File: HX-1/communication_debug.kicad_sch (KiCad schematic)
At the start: 0 parts

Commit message: move components to correct sheets, change net labels to global
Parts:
- added D1, D2: D_Schottky, symbol Device:D_Schottky
- added JP1: 5V_USB_Solder_Bridge, Jumper:SolderJumper-2_P1.3mm_Bridged_RoundedPad1.0x1.5mm, symbol Jumper:SolderJumper_2_Bridged
- added P1: USB_C_Plug_USB2.0, symbol Connector:USB_C_Plug_USB2.0
- added R2: 10k, Resistor_SMD:R_0603_1608Metric, symbol Device:R
- added R3: 20k, Resistor_SMD:R_0603_1608Metric, symbol Device:R
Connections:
- new net: D1.1 (K), JP1.1 (A)
- new net +5V: JP1.2 (B)
- new net GND: P1.A1 (GND), P1.A12 (GND), P1.B1 (GND), P1.B12 (GND), R3.2
- new net USB_FS_D+: P1.A6 (D+)
- new net USB_FS_D-: P1.A7 (D-)
- new net USB_VBUS_Sensing: D2.1 (K)
- new net VBUS: D1.2 (A), P1.A4 (VBUS), P1.A9 (VBUS), P1.B4 (VBUS), P1.B9 (VBUS), R2.1
- new net vbus_r_divider: D2.2 (A), R2.2, R3.1
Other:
- note added: "TODO: add VBUS LED"

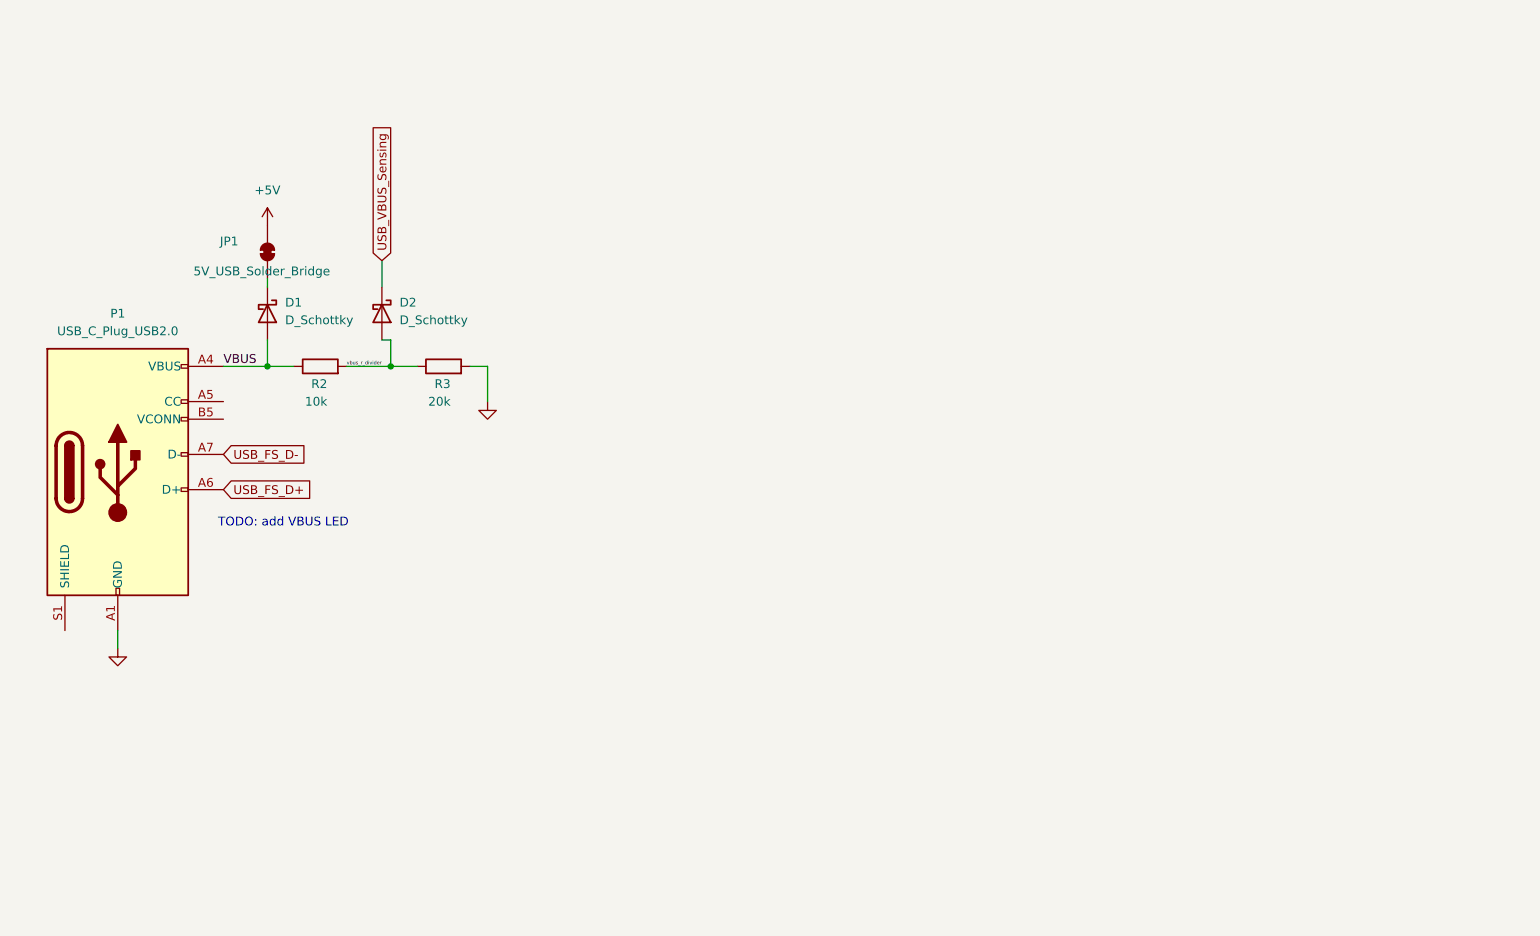
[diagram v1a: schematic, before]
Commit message: add first draft of USB C design
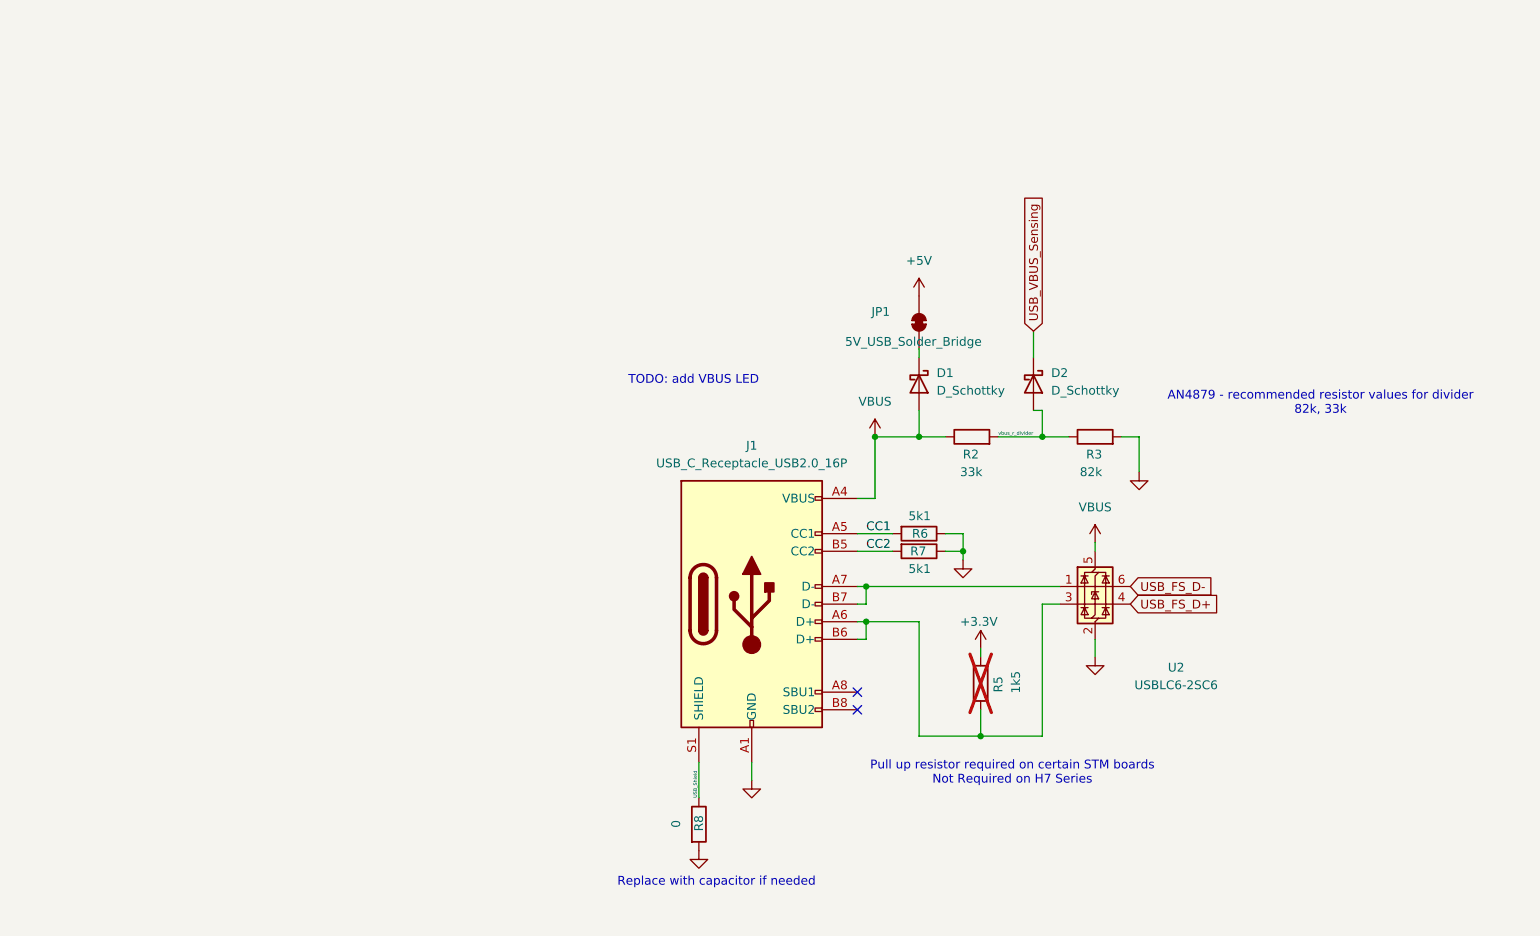
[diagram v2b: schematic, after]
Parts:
- removed P1: USB_C_Plug_USB2.0, symbol Connector:USB_C_Plug_USB2.0
- added J1: USB_C_Receptacle_USB2.0_16P, Connector_USB:USB_C_Receptacle_G-Switch_GT-USB-7010ASV, symbol Connector:USB_C_Receptacle_USB2.0_16P
- added R5: 1k5, Resistor_SMD:R_0603_1608Metric, symbol Device:R
- added R6, R7: 5k1, Resistor_SMD:R_0603_1608Metric, symbol Device:R
- added R8: 0, Resistor_SMD:R_0603_1608Metric, symbol Device:R
- added U2: USBLC6-2SC6, Package_TO_SOT_SMD:SOT-23-6, symbol Power_Protection:USBLC6-2SC6
- D1, D2: footprint (none) -> Diode_SMD:D_SOD-323F; LCSC PN (none) -> C146335
- R2: value 10k -> 33k; LCSC PN C3017715 -> (none)
- R3: value 20k -> 82k
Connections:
- net GND: now also J1.A1 (GND), J1.A12 (GND), J1.B1 (GND), J1.B12 (GND), R6.1, R7.1, R8.2, U2.2 (GND)
- net USB_FS_D+: now also U2.4 (I/O2)
- net USB_FS_D-: now also U2.6 (I/O1)
- net VBUS: now also J1.A4 (VBUS), J1.A9 (VBUS), J1.B4 (VBUS), J1.B9 (VBUS), U2.5 (VBUS)
- new net: J1.A6 (D+), J1.B6 (D+), R5.1, U2.3 (I/O2)
- new net: J1.A7 (D-), J1.B7 (D-), U2.1 (I/O1)
- new net +3.3V: R5.2
- new net CC1: J1.A5 (CC1), R6.2
- new net CC2: J1.B5 (CC2), R7.2
- new net USB_Shield: J1.S1 (SHIELD), R8.1
- no-connect marks 0 -> 2
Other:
- note added: "AN4879 - recommended resistor values for divider 82k, 33k"
- note added: "Pull up resistor required on certain STM boards Not Required on H7 Series"
- note added: "Replace with capacitor if needed"
- moved on the sheet: JP1, R2, R3

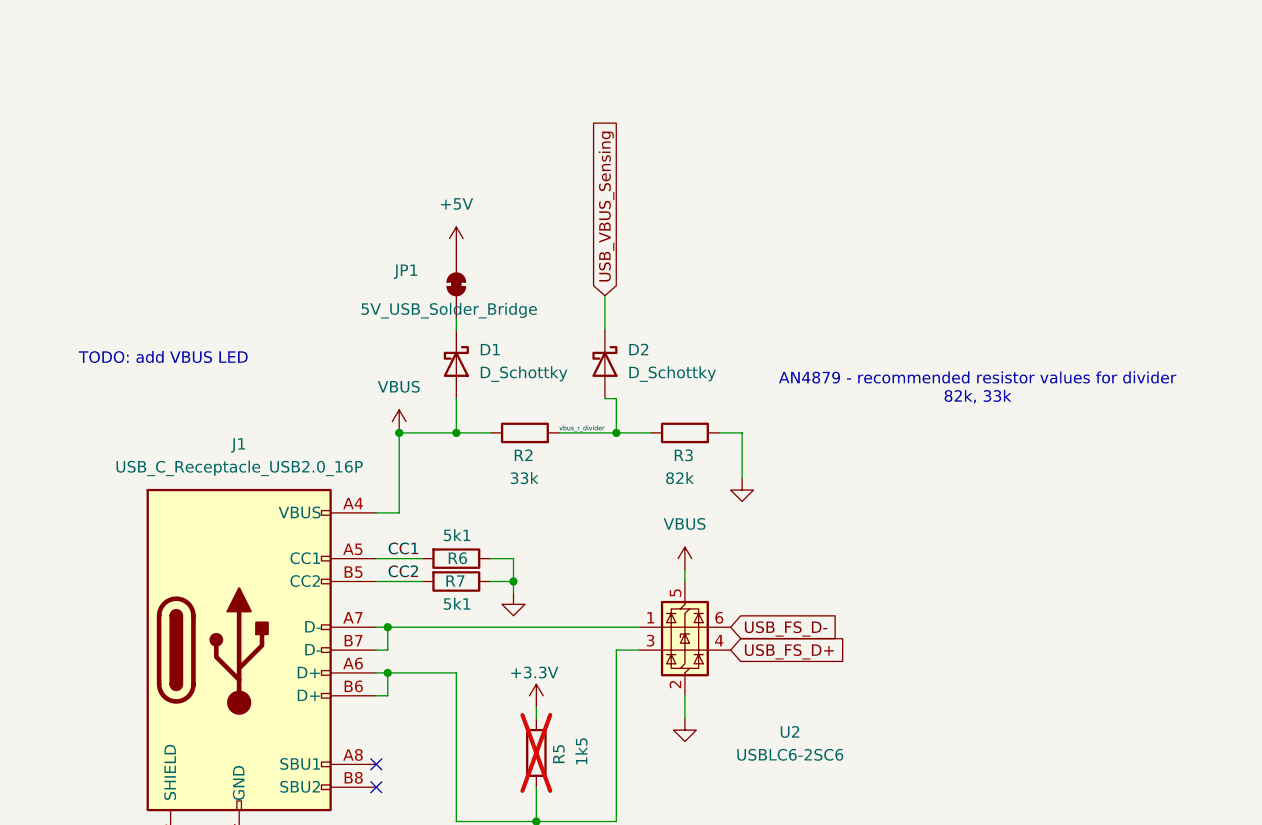
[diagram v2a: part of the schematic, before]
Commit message: add LED and remaining footprints/LCSC PN to USB C circuit
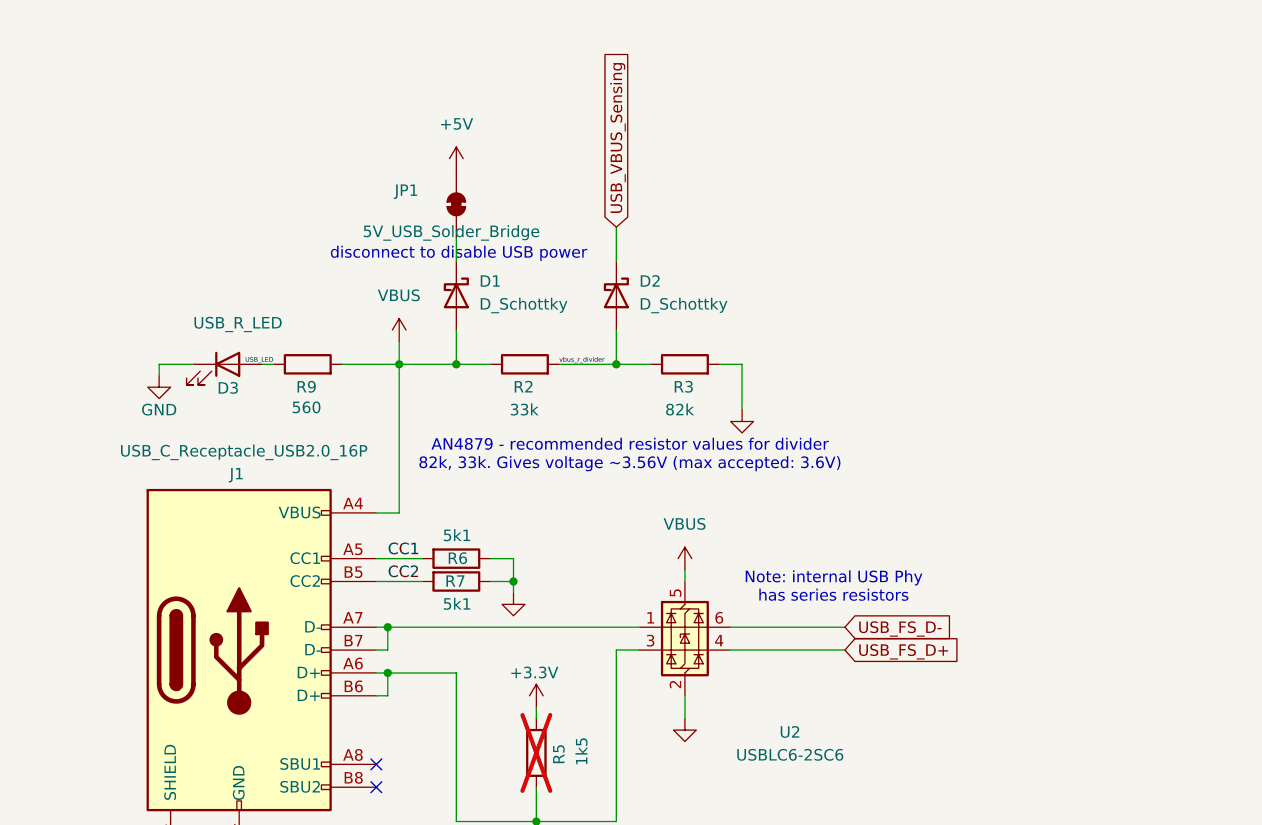
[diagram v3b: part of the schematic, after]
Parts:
- added D3: USB_R_LED, LED_SMD:LED_0603_1608Metric, symbol Device:LED
- added R9: 560, Resistor_SMD:R_0603_1608Metric, symbol Device:R
- R2: LCSC PN (none) -> C4216
- R3: LCSC PN (none) -> C23254
- R6, R7: LCSC PN (none) -> C23186
- R8: LCSC PN (none) -> C21189
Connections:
- net GND: now also D3.1 (K)
- net VBUS: now also R9.2
- new net USB_LED: D3.2 (A), R9.1
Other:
- note added: "AN4879 - recommended resistor values for divider 82k, 33k. Gives voltage ~3.56V (max accepted: 3.6V)"
- note added: "Note: internal USB Phy has series resistors"
- note added: "disconnect to disable USB power"
- note removed: "AN4879 - recommended resistor values for divider 82k, 33k"
- note removed: "TODO: add VBUS LED"
- moved on the sheet: D1, D2, JP1, R2, R3

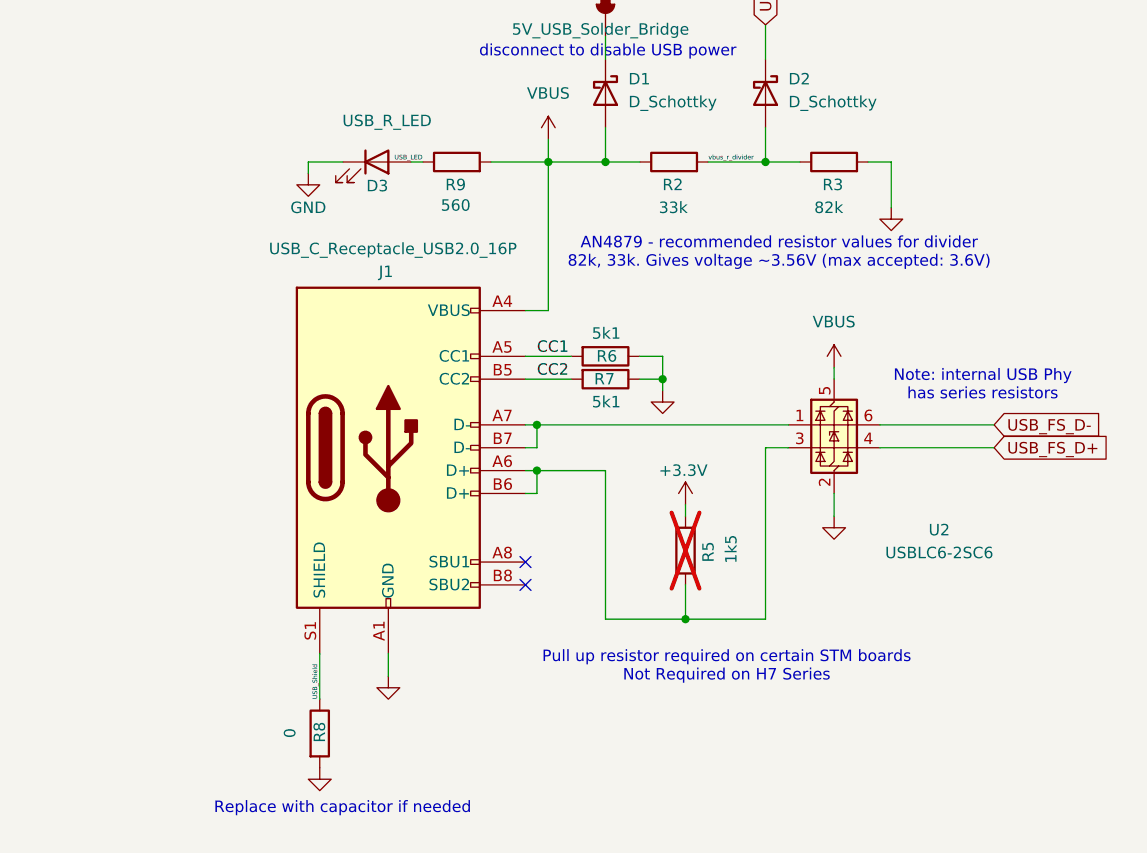
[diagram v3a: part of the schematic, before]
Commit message: add vbus filtering and voltage regululator for 3.3V
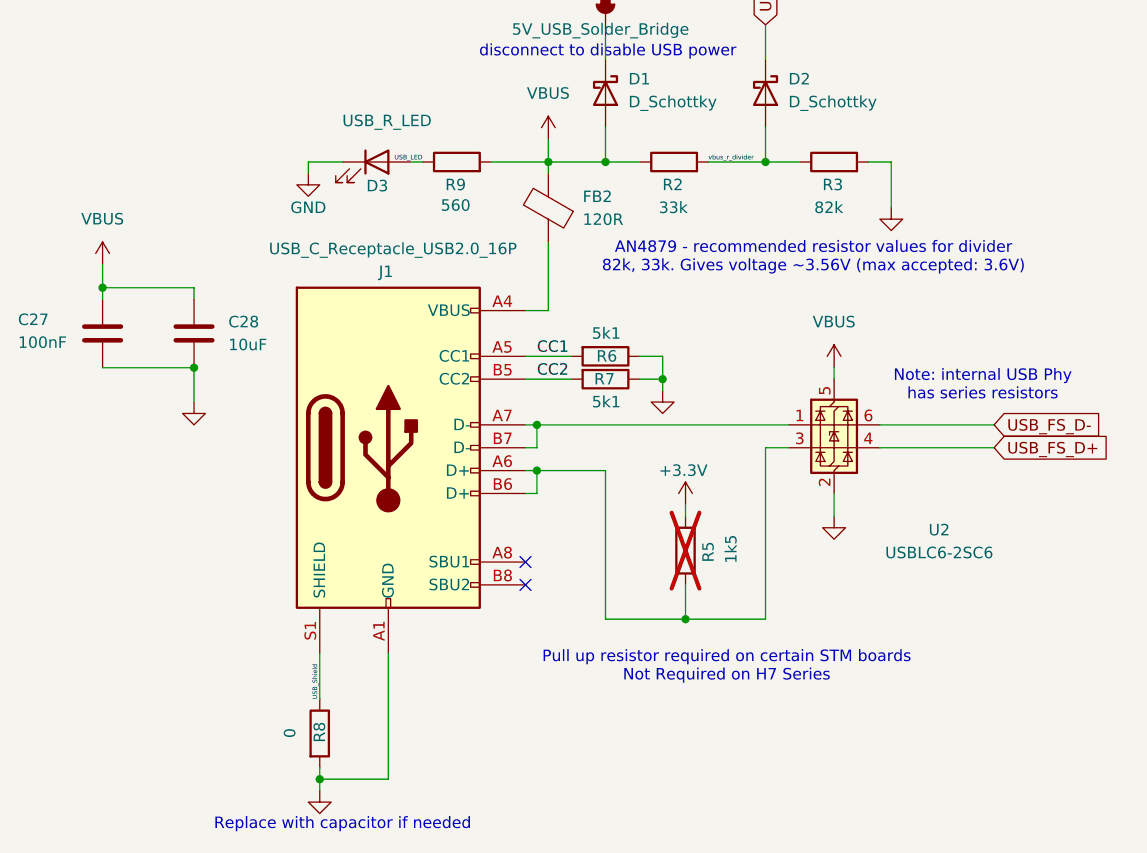
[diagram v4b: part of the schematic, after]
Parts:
- added C27: 100nF, Capacitor_SMD:C_0603_1608Metric, symbol Device:C
- added C28: 10uF, Capacitor_SMD:C_0603_1608Metric, symbol Device:C
- added FB2: 120R, Resistor_SMD:R_0603_1608Metric, symbol Device:FerriteBead
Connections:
- net GND: now also C27.1, C28.2
- net VBUS: now also C27.2, C28.1, FB2.2; no longer J1.A4 (VBUS), J1.A9 (VBUS), J1.B4 (VBUS), J1.B9 (VBUS)
- new net: FB2.1, J1.A4 (VBUS), J1.A9 (VBUS), J1.B4 (VBUS), J1.B9 (VBUS)

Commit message: change almost all components to be basic jlcpcb parts
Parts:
- C27: LCSC PN C478888 -> C14663
- C28: LCSC PN C70225 -> C19702
- FB2: value 120R -> 100R; footprint Resistor_SMD:R_0603_1608Metric -> Resistor_SMD:R_0805_2012Metric; LCSC PN C280478 -> C1015
- R9: value 560 -> 1k; LCSC PN C23204 -> C21190
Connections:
- net VBUS: now also FB2.1; no longer FB2.2
- net at J1.A4 (VBUS), J1.A9 (VBUS), J1.B4 (VBUS)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: now also FB2.2; no longer FB2.1
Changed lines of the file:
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@@
+	)
+	(symbol
+		(lib_id "Device:FerriteBead")
+		(at 143.51 80.01 0)
+		(unit 1)
+		(exclude_from_sim no)
+		(in_bom yes)
+		(on_board yes)
+		(dnp no)
+		(fields_autoplaced yes)
+		(property "Reference" "FB2"
+			(at 147.32 78.6891 0)
+			(effects
+				(font
+					(size 1.27 1.27)
+				)
+				(justify left)
+			)
+		)
+		(property "Value" "100R"
+			(at 147.32 81.2291 0)
+			(effects
+				(font
+					(size 1.27 1.27)
+				)
+				(justify left)
+			)
+		)
+		(property "Footprint" "Resistor_SMD:R_0805_2012Metric"
+			(at 141.732 80.01 90)
+			(effects
+				(font
+					(size 1.27 1.27)
+				)
+				(hide yes)
+			)
+		)
+		(property "Datasheet" "~"
+			(at 143.51 80.01 0)
+			(effects
+				(font
+					(size 1.27 1.27)
+				)
+				(hide yes)
+			)
+		)
+		(property "Description" "Ferrite bead"
+			(at 143.51 80.01 0)
+			(effects
+				(font
+					(size 1.27 1.27)
+				)
+				(hide yes)
+			)
+		)
+		(property "LCSC PN" "C1015"
+			(at 143.51 80.01 0)
+			(effects
+				(font
+					(size 1.27 1.27)
+				)
+				(hide yes)
+			)
+		)
+		(pin "2"
+		)
+		(pin "1"
+		)
+		(instances
+			(project "HX-1"
+				(path "/a3219989-2bf1-44ea-9412-fab86edfb39b/f68304e7-586c-4481-9c91-394c7e636be5"
+					(reference "FB2")
+					(unit 1)
+				)
+			)
+		)
 	)
 	(symbol
@@
 			)
 		)
-		(property "LCSC PN" "C70225"
+		(property "LCSC PN" "C19702"
 			(at 104.14 93.98 0)
 			(effects
@@
 			)
 		)
-		(property "Value" "560"
+		(property "Value" "1k"
 			(at 134.874 79.756 90)
 			(effects
@@
 			)
 		)
-		(property "LCSC PN" "C23204"
+		(property "LCSC PN" "C21190"
 			(at 133.35 74.93 0)
 			(effects
@@
 				(path "/a3219989-2bf1-44ea-9412-fab86edfb39b/f68304e7-586c-4481-9c91-394c7e636be5"
 					(reference "R9")
-					(unit 1)
-				)
-			)
-		)
-	)
-	(symbol
-		(lib_id "Device:FerriteBead")
-		(at 143.51 80.01 180)
-		(unit 1)
-		(exclude_from_sim no)
-		(in_bom yes)
-		(on_board yes)
-		(dnp no)
-		(fields_autoplaced yes)
-		(property "Reference" "FB2"
-			(at 147.32 78.7907 0)
-			(effects
-				(font
-					(size 1.27 1.27)
-				)
-				(justify right)
-			)
-		)
-		(property "Value" "120R"
-			(at 147.32 81.3307 0)
-			(effects
-				(font
-					(size 1.27 1.27)
-				)
-				(justify right)
-			)
-		)
-		(property "Footprint" "Resistor_SMD:R_0603_1608Metric"
-			(at 145.288 80.01 90)
-			(effects
-				(font
-					(size 1.27 1.27)
-				)
-				(hide yes)
-			)
-		)
-		(property "Datasheet" "~"
-			(at 143.51 80.01 0)
-			(effects
-				(font
-					(size 1.27 1.27)
-				)
-				(hide yes)
-			)
-		)
-		(property "Description" "Ferrite bead"
-			(at 143.51 80.01 0)
-			(effects
-				(font
-					(size 1.27 1.27)
-				)
-				(hide yes)
-			)
-		)
-		(property "LCSC PN" "C280478"
-			(at 143.51 80.01 0)
-			(effects
-				(font
-					(size 1.27 1.27)
-				)
-				(hide yes)
-			)
-		)
-		(pin "2"
-		)
-		(pin "1"
-		)
-		(instances
-			(project "HX-1"
-				(path "/a3219989-2bf1-44ea-9412-fab86edfb39b/f68304e7-586c-4481-9c91-394c7e636be5"
-					(reference "FB2")
 					(unit 1)
 				)
@@
 			)
 		)
-		(property "LCSC PN" "C478888"
+		(property "LCSC PN" "C14663"
 			(at 93.98 93.98 0)
 			(effects
